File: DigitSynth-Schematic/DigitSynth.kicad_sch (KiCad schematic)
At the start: 0 parts

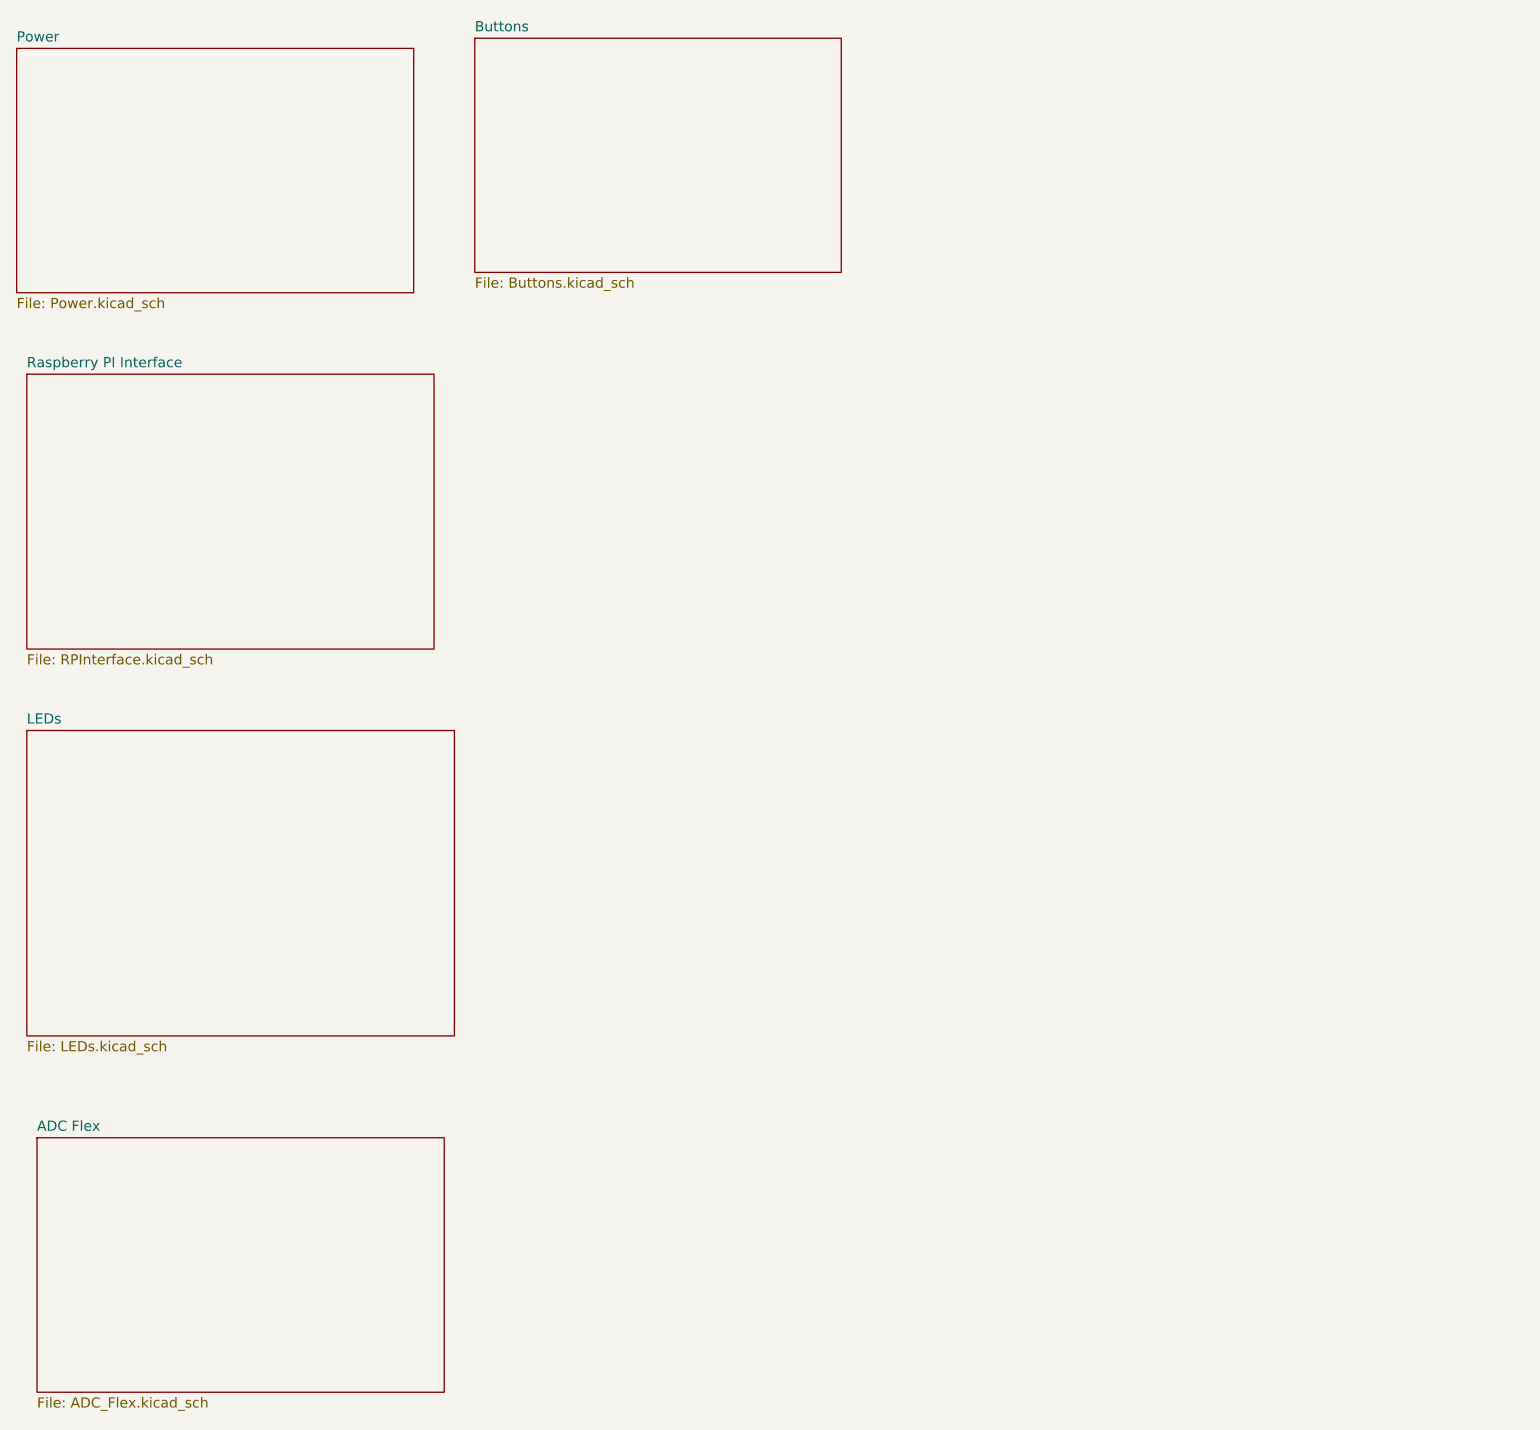
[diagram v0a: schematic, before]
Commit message: Add completed KiCad schematic hierarchy (Pi interface, ADC, LEDs, buttons, power)
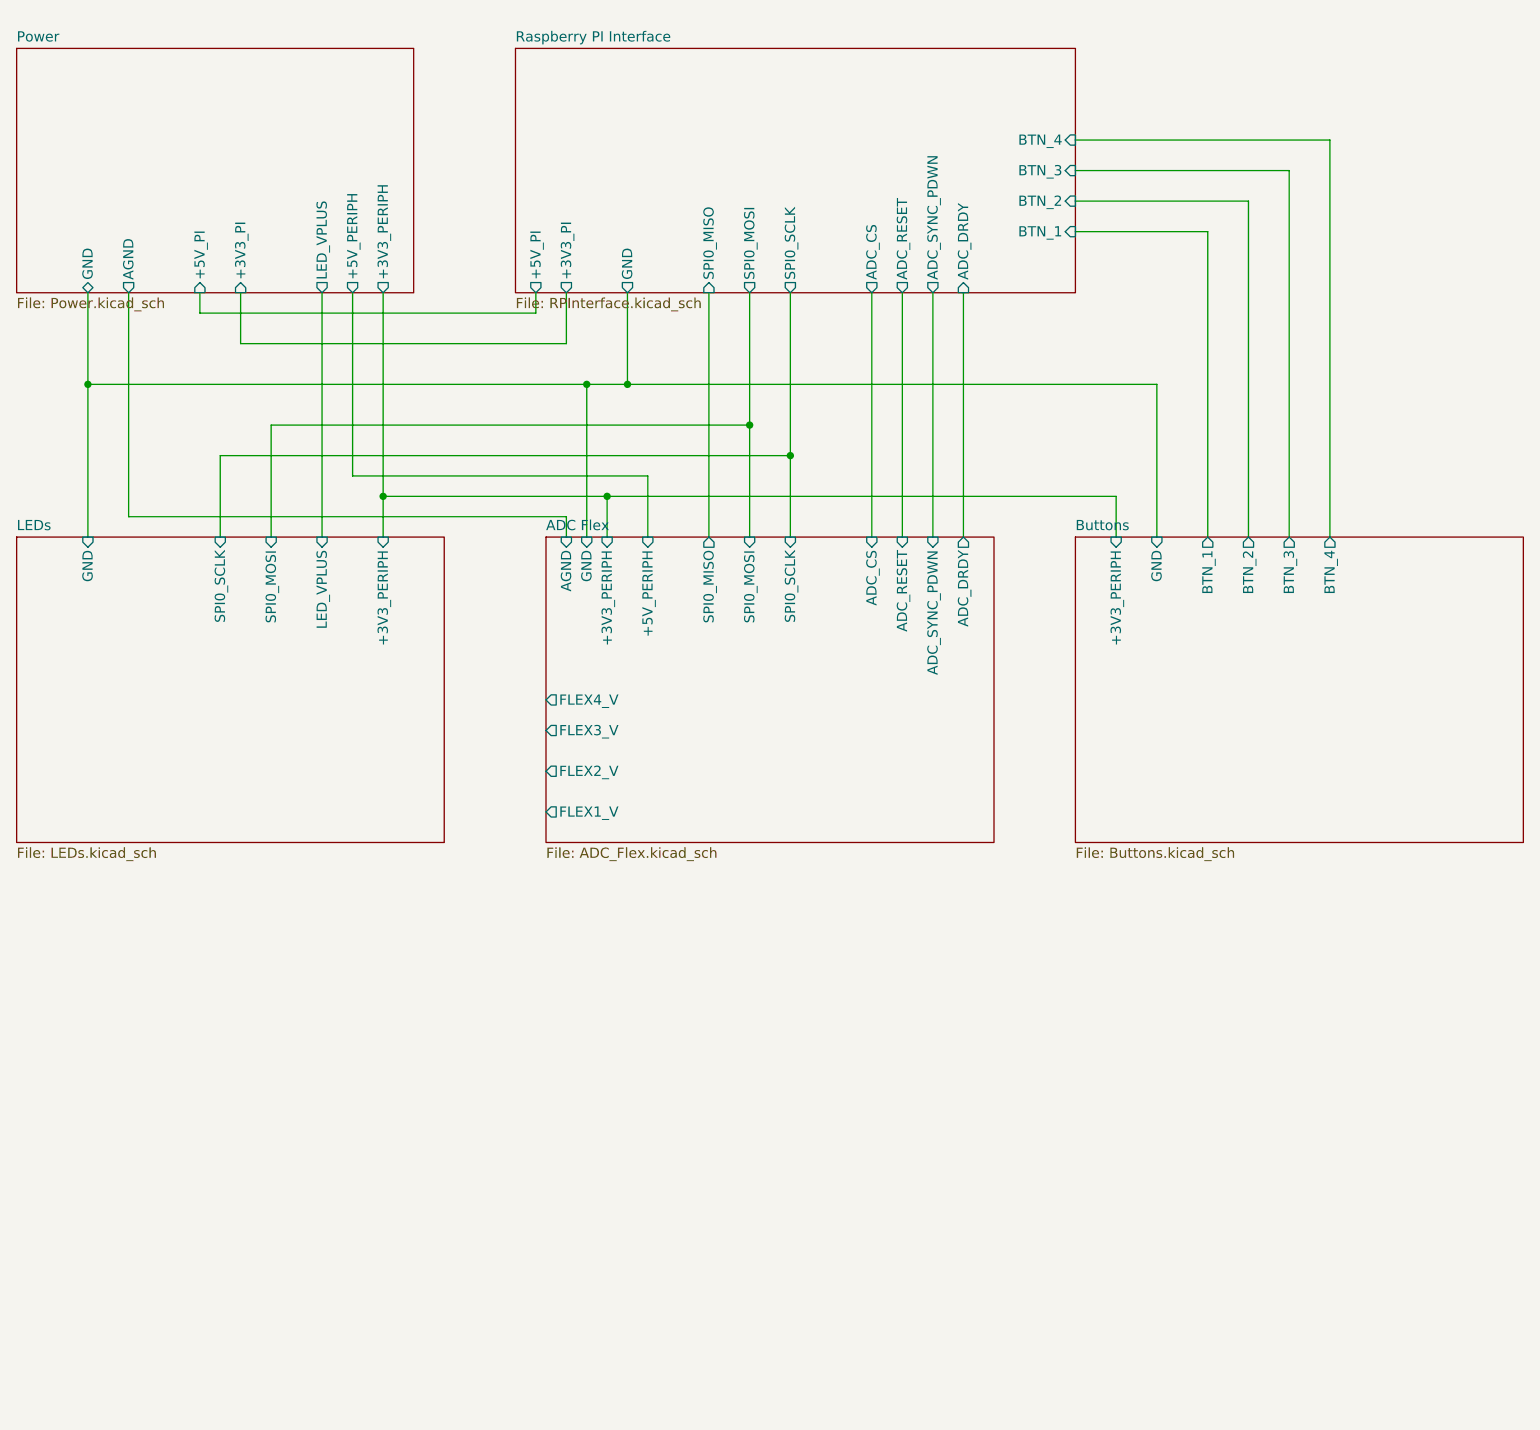
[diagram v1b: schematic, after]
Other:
- sheet ADC Flex ports: added +3V3_PERIPH, +5V_PERIPH, ADC_CS, ADC_DRDY, ADC_RESET, ADC_SYNC_PDWN, AGND, FLEX1_V, FLEX2_V, FLEX3_V, FLEX4_V, GND, SPI0_MISO, SPI0_MOSI, SPI0_SCLK; removed none
- sheet Buttons ports: added +3V3_PERIPH, BTN_1, BTN_2, BTN_3, BTN_4, GND; removed none
- sheet LEDs ports: added +3V3_PERIPH, GND, LED_VPLUS, SPI0_MOSI, SPI0_SCLK; removed none
- sheet Power ports: added +3V3_PERIPH, +3V3_PI, +5V_PERIPH, +5V_PI, AGND, GND, LED_VPLUS; removed none
- sheet Raspberry PI Interface ports: added +3V3_PI, +5V_PI, ADC_CS, ADC_DRDY, ADC_RESET, ADC_SYNC_PDWN, BTN_1, BTN_2, BTN_3, BTN_4, GND, SPI0_MISO, SPI0_MOSI, SPI0_SCLK; removed none
